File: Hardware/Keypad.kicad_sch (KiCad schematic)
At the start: 35 parts, among them SW1 MX1A-E1NW, SW10 MX1A-E1NW, SW11 MX1A-E1NW, SW12 MX1A-E1NW, SW13 RESET, SW2 MX1A-E1NW, SW3 MX1A-E1NW, SW4 MX1A-E1NW, SW5 MX1A-E1NW, SW6 MX1A-E1NW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

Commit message: minor improvements to PCB design
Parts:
- D13, D14: footprint LED_SMD:LED_0603_1608Metric_Pad1.05x0.95mm_HandSolder -> LED_SMD:LED_0603_1608Metric
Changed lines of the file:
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@@
     (property "Reference" "D14" (id 0) (at 64.77 142.24 0))
     (property "Value" "LED" (id 1) (at 64.77 147.32 0))
-    (property "Footprint" "LED_SMD:LED_0603_1608Metric_Pad1.05x0.95mm_HandSolder" (id 2) (at 64.77 144.78 0)
+    (property "Footprint" "LED_SMD:LED_0603_1608Metric" (id 2) (at 64.77 144.78 0)
       (effects (font (size 1.27 1.27)) hide)
     )
@@
     (property "Reference" "D13" (id 0) (at 64.77 132.08 0))
     (property "Value" "LED" (id 1) (at 64.77 137.16 0))
-    (property "Footprint" "LED_SMD:LED_0603_1608Metric_Pad1.05x0.95mm_HandSolder" (id 2) (at 64.77 134.62 0)
+    (property "Footprint" "LED_SMD:LED_0603_1608Metric" (id 2) (at 64.77 134.62 0)
       (effects (font (size 1.27 1.27)) hide)
     )
@@
     )
     (path "/f4e1b81e-f02a-451a-905f-f000b6b75e92"
-      (reference "D13") (unit 1) (value "LED") (footprint "LED_SMD:LED_0603_1608Metric_Pad1.05x0.95mm_HandSolder")
+      (reference "D13") (unit 1) (value "LED") (footprint "LED_SMD:LED_0603_1608Metric")
     )
     (path "/e7f7fe4f-ebfb-471a-976d-2ea6e6769e03"
-      (reference "D14") (unit 1) (value "LED") (footprint "LED_SMD:LED_0603_1608Metric_Pad1.05x0.95mm_HandSolder")
+      (reference "D14") (unit 1) (value "LED") (footprint "LED_SMD:LED_0603_1608Metric")
     )
     (path "/dc9e1614-34a9-4e22-a9cf-c8e55ec48f0f"

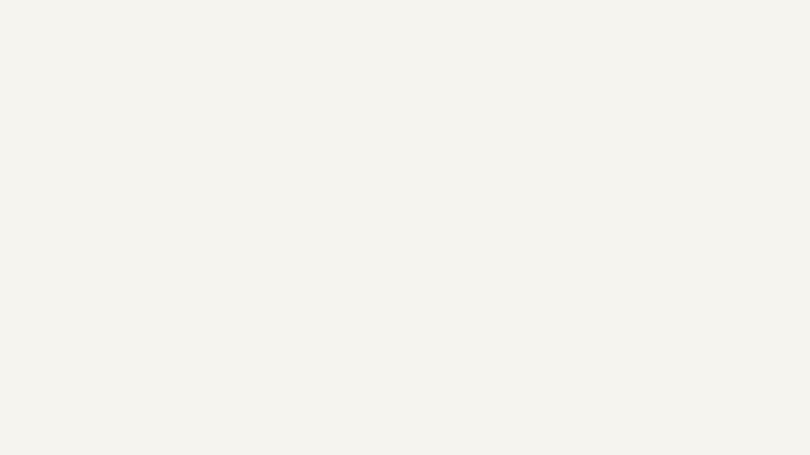
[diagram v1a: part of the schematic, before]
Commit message: replaced mounting holes with grounded pads
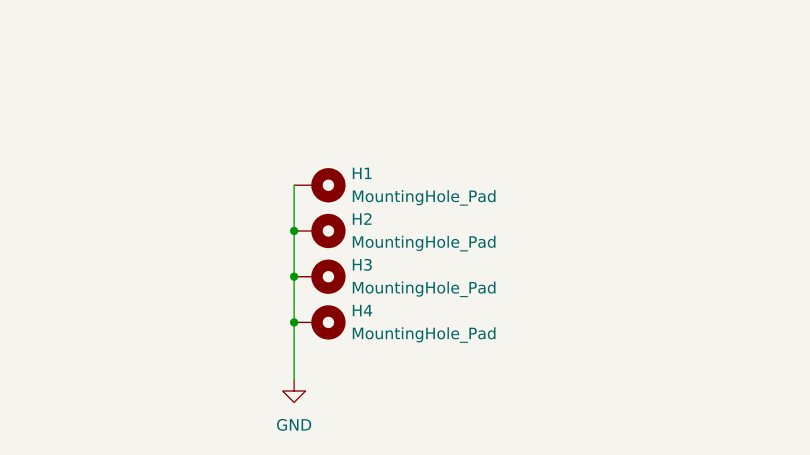
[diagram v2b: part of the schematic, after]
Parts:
- added H1, H2, H3, H4: MountingHole_Pad, MountingHole:MountingHole_2.7mm_M2.5_Pad, symbol Mechanical:MountingHole_Pad
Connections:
- net GND: now also H1.1, H2.1, H3.1, H4.1
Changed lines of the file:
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@@
   (junction (at 198.12 114.3) (diameter 0) (color 0 0 0 0)
   )
+  (junction (at 110.49 175.26) (diameter 0) (color 0 0 0 0)
+  )
   (junction (at 67.31 92.71) (diameter 0) (color 0 0 0 0)
   )
@@
   (junction (at 250.19 87.63) (diameter 0) (color 0 0 0 0)
   )
+  (junction (at 110.49 170.18) (diameter 0) (color 0 0 0 0)
+  )
   (junction (at 85.09 96.52) (diameter 0) (color 0 0 0 0)
   )
@@
   (junction (at 236.22 114.3) (diameter 0) (color 0 0 0 0)
   )
+  (junction (at 110.49 165.1) (diameter 0) (color 0 0 0 0)
+  )
   (junction (at 218.44 106.68) (diameter 0) (color 0 0 0 0)
   )
@@
     (stroke (width 0) (type default) (color 0 0 0 0))
   )
+  (wire (pts (xy 110.49 160.02) (xy 110.49 165.1))
+    (stroke (width 0) (type default) (color 0 0 0 0))
+  )
   (wire (pts (xy 66.04 66.04) (xy 67.31 66.04))
     (stroke (width 0) (type default) (color 0 0 0 0))
@@
     (stroke (width 0) (type default) (color 0 0 0 0))
   )
+  (wire (pts (xy 110.49 175.26) (xy 110.49 181.61))
+    (stroke (width 0) (type default) (color 0 0 0 0))
+  )
   (wire (pts (xy 250.19 72.39) (xy 250.19 87.63))
     (stroke (width 0) (type default) (color 0 0 0 0))
@@
     (stroke (width 0) (type default) (color 0 0 0 0))
   )
+  (wire (pts (xy 110.49 170.18) (xy 110.49 175.26))
+    (stroke (width 0) (type default) (color 0 0 0 0))
+  )
   (wire (pts (xy 198.12 125.73) (xy 195.58 125.73))
     (stroke (width 0) (type default) (color 0 0 0 0))
@@
   )
   (wire (pts (xy 198.12 95.25) (xy 236.22 95.25))
+    (stroke (width 0) (type default) (color 0 0 0 0))
+  )
+  (wire (pts (xy 110.49 165.1) (xy 110.49 170.18))
     (stroke (width 0) (type default) (color 0 0 0 0))
   )
@@
     (pin "2")
   )
+  (symbol (lib_id "Mechanical:MountingHole_Pad") (at 113.03 160.02 270) (unit 1)
+    (in_bom yes) (on_board yes) (fields_autoplaced)
+    (property "Reference" "H1" (id 0) (at 116.84 158.7499 90)
+      (effects (font (size 1.27 1.27)) (justify left))
+    )
+    (property "Value" "MountingHole_Pad" (id 1) (at 116.84 161.2899 90)
+      (effects (font (size 1.27 1.27)) (justify left))
+    )
+    (property "Footprint" "MountingHole:MountingHole_2.7mm_M2.5_Pad" (id 2) (at 113.03 160.02 0)
+      (effects (font (size 1.27 1.27)) hide)
+    )
+    (property "Datasheet" "~" (id 3) (at 113.03 160.02 0)
+      (effects (font (size 1.27 1.27)) hide)
+    )
+    (pin "1")
+  )
   (symbol (lib_id "Diode:1N4148") (at 267.97 110.49 90) (unit 1)
     (in_bom yes) (on_board yes) (fields_autoplaced)
@@
     (pin "2")
   )
+  (symbol (lib_id "power:GND") (at 110.49 181.61 0) (unit 1)
+    (in_bom yes) (on_board yes) (fields_autoplaced)
+    (property "Reference" "#PWR0105" (id 0) (at 110.49 187.96 0)
+      (effects (font (size 1.27 1.27)) hide)
+    )
+    (property "Value" "GND" (id 1) (at 110.49 186.69 0))
+    (property "Footprint" "" (id 2) (at 110.49 181.61 0)
+      (effects (font (size 1.27 1.27)) hide)
+    )
+    (property "Datasheet" "" (id 3) (at 110.49 181.61 0)
+      (effects (font (size 1.27 1.27)) hide)
+    )
+    (pin "1")
+  )
   (symbol (lib_id "Diode:1N4148") (at 236.22 129.54 90) (unit 1)
     (in_bom yes) (on_board yes) (fields_autoplaced)
@@
     (pin "1")
     (pin "2")
+  )
+  (symbol (lib_id "Mechanical:MountingHole_Pad") (at 113.03 170.18 270) (unit 1)
+    (in_bom yes) (on_board yes) (fields_autoplaced)
+    (property "Reference" "H3" (id 0) (at 116.84 168.9099 90)
+      (effects (font (size 1.27 1.27)) (justify left))
+    )
+    (property "Value" "MountingHole_Pad" (id 1) (at 116.84 171.4499 90)
+      (effects (font (size 1.27 1.27)) (justify left))
+    )
+    (property "Footprint" "MountingHole:MountingHole_2.7mm_M2.5_Pad" (id 2) (at 113.03 170.18 0)
+      (effects (font (size 1.27 1.27)) hide)
+    )
+    (property "Datasheet" "~" (id 3) (at 113.03 170.18 0)
+      (effects (font (size 1.27 1.27)) hide)
+    )
+    (pin "1")
   )
   (symbol (lib_id "Switch:SW_Push") (at 60.96 66.04 0) (unit 1)
@@
     (pin "2")
   )
+  (symbol (lib_id "Mechanical:MountingHole_Pad") (at 113.03 175.26 270) (unit 1)
+    (in_bom yes) (on_board yes) (fields_autoplaced)
+    (property "Reference" "H4" (id 0) (at 116.84 173.9899 90)
+      (effects (font (size 1.27 1.27)) (justify left))
+    )
+    (property "Value" "MountingHole_Pad" (id 1) (at 116.84 176.5299 90)
+      (effects (font (size 1.27 1.27)) (justify left))
+    )
+    (property "Footprint" "MountingHole:MountingHole_2.7mm_M2.5_Pad" (id 2) (at 113.03 175.26 0)
+      (effects (font (size 1.27 1.27)) hide)
+    )
+    (property "Datasheet" "~" (id 3) (at 113.03 175.26 0)
+      (effects (font (size 1.27 1.27)) hide)
+    )
+    (pin "1")
+  )
   (symbol (lib_id "power:+3V3") (at 85.09 96.52 0) (unit 1)
     (in_bom yes) (on_board yes) (fields_autoplaced)
@@
     )
     (property "Datasheet" "" (id 3) (at 85.09 96.52 0)
+      (effects (font (size 1.27 1.27)) hide)
+    )
+    (pin "1")
+  )
+  (symbol (lib_id "Mechanical:MountingHole_Pad") (at 113.03 165.1 270) (unit 1)
+    (in_bom yes) (on_board yes) (fields_autoplaced)
+    (property "Reference" "H2" (id 0) (at 116.84 163.8299 90)
+      (effects (font (size 1.27 1.27)) (justify left))
+    )
+    (property "Value" "MountingHole_Pad" (id 1) (at 116.84 166.3699 90)
+      (effects (font (size 1.27 1.27)) (justify left))
+    )
+    (property "Footprint" "MountingHole:MountingHole_2.7mm_M2.5_Pad" (id 2) (at 113.03 165.1 0)
+      (effects (font (size 1.27 1.27)) hide)
+    )
+    (property "Datasheet" "~" (id 3) (at 113.03 165.1 0)
       (effects (font (size 1.27 1.27)) hide)
     )
@@
       (reference "#PWR0104") (unit 1) (value "GND") (footprint "")
     )
+    (path "/4c41d73b-9629-4891-9f71-d307bc169690"
+      (reference "#PWR0105") (unit 1) (value "GND") (footprint "")
+    )
     (path "/9b5a0617-70c8-4bdd-b9f5-190c8f0a9438"
       (reference "D1") (unit 1) (value "1N4148") (footprint "Diode_SMD:D_MELF")
@@
       (reference "D14") (unit 1) (value "LED") (footprint "LED_SMD:LED_0603_1608Metric")
     )
+    (path "/2abf9bd9-2e75-4bc7-9218-8b355c67c085"
+      (reference "H1") (unit 1) (value "MountingHole_Pad") (footprint "MountingHole:MountingHole_2.7mm_M2.5_Pad")
+    )
+    (path "/abba4978-3a4b-4852-b54b-6b91e24103c3"
+      (reference "H2") (unit 1) (value "MountingHole_Pad") (footprint "MountingHole:MountingHole_2.7mm_M2.5_Pad")
+    )
+    (path "/75202622-1795-44f1-83e8-a3062aaae217"
+      (reference "H3") (unit 1) (value "MountingHole_Pad") (footprint "MountingHole:MountingHole_2.7mm_M2.5_Pad")
+    )
+    (path "/9f0df0db-34ed-4aca-8400-a4bc646665f9"
+      (reference "H4") (unit 1) (value "MountingHole_Pad") (footprint "MountingHole:MountingHole_2.7mm_M2.5_Pad")
+    )
     (path "/dc9e1614-34a9-4e22-a9cf-c8e55ec48f0f"

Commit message: updated diode footprints to MiniMELF
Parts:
- D1, D10, D11, D12, D2, D3, D4, D5, D6, D7, D8, D9: footprint Diode_SMD:D_MELF -> Diode_SMD:D_MiniMELF
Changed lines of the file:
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@@
       (effects (font (size 1.27 1.27)) (justify right))
     )
-    (property "Footprint" "Diode_SMD:D_MELF" (id 2) (at 272.415 129.54 0)
+    (property "Footprint" "Diode_SMD:D_MiniMELF" (id 2) (at 272.415 129.54 0)
       (effects (font (size 1.27 1.27)) hide)
     )
@@
       (effects (font (size 1.27 1.27)) (justify right))
     )
-    (property "Footprint" "Diode_SMD:D_MELF" (id 2) (at 272.415 110.49 0)
+    (property "Footprint" "Diode_SMD:D_MiniMELF" (id 2) (at 272.415 110.49 0)
       (effects (font (size 1.27 1.27)) hide)
     )
@@
       (effects (font (size 1.27 1.27)) (justify right))
     )
-    (property "Footprint" "Diode_SMD:D_MELF" (id 2) (at 240.665 129.54 0)
+    (property "Footprint" "Diode_SMD:D_MiniMELF" (id 2) (at 240.665 129.54 0)
       (effects (font (size 1.27 1.27)) hide)
     )
@@
       (effects (font (size 1.27 1.27)) (justify right))
     )
-    (property "Footprint" "Diode_SMD:D_MELF" (id 2) (at 202.565 91.44 0)
+    (property "Footprint" "Diode_SMD:D_MiniMELF" (id 2) (at 202.565 91.44 0)
       (effects (font (size 1.27 1.27)) hide)
     )
@@
       (effects (font (size 1.27 1.27)) (justify right))
     )
-    (property "Footprint" "Diode_SMD:D_MELF" (id 2) (at 164.465 91.44 0)
+    (property "Footprint" "Diode_SMD:D_MiniMELF" (id 2) (at 164.465 91.44 0)
       (effects (font (size 1.27 1.27)) hide)
     )
@@
       (effects (font (size 1.27 1.27)) (justify right))
     )
-    (property "Footprint" "Diode_SMD:D_MELF" (id 2) (at 164.465 110.49 0)
+    (property "Footprint" "Diode_SMD:D_MiniMELF" (id 2) (at 164.465 110.49 0)
       (effects (font (size 1.27 1.27)) hide)
     )
@@
       (effects (font (size 1.27 1.27)) (justify right))
     )
-    (property "Footprint" "Diode_SMD:D_MELF" (id 2) (at 202.565 110.49 0)
+    (property "Footprint" "Diode_SMD:D_MiniMELF" (id 2) (at 202.565 110.49 0)
       (effects (font (size 1.27 1.27)) hide)
     )
@@
       (effects (font (size 1.27 1.27)) (justify right))
     )
-    (property "Footprint" "Diode_SMD:D_MELF" (id 2) (at 272.415 91.44 0)
+    (property "Footprint" "Diode_SMD:D_MiniMELF" (id 2) (at 272.415 91.44 0)
       (effects (font (size 1.27 1.27)) hide)
     )
@@
       (effects (font (size 1.27 1.27)) (justify right))
     )
-    (property "Footprint" "Diode_SMD:D_MELF" (id 2) (at 240.665 110.49 0)
+    (property "Footprint" "Diode_SMD:D_MiniMELF" (id 2) (at 240.665 110.49 0)
       (effects (font (size 1.27 1.27)) hide)
     )
@@
       (effects (font (size 1.27 1.27)) (justify right))
     )
-    (property "Footprint" "Diode_SMD:D_MELF" (id 2) (at 240.665 91.44 0)
+    (property "Footprint" "Diode_SMD:D_MiniMELF" (id 2) (at 240.665 91.44 0)
       (effects (font (size 1.27 1.27)) hide)
     )
@@
       (effects (font (size 1.27 1.27)) (justify right))
     )
-    (property "Footprint" "Diode_SMD:D_MELF" (id 2) (at 202.565 129.54 0)
+    (property "Footprint" "Diode_SMD:D_MiniMELF" (id 2) (at 202.565 129.54 0)
       (effects (font (size 1.27 1.27)) hide)
     )
@@
       (effects (font (size 1.27 1.27)) (justify right))
     )
-    (property "Footprint" "Diode_SMD:D_MELF" (id 2) (at 164.465 129.54 0)
+    (property "Footprint" "Diode_SMD:D_MiniMELF" (id 2) (at 164.465 129.54 0)
       (effects (font (size 1.27 1.27)) hide)
     )
@@
     )
     (path "/9b5a0617-70c8-4bdd-b9f5-190c8f0a9438"
-      (reference "D1") (unit 1) (value "1N4148") (footprint "Diode_SMD:D_MELF")
+      (reference "D1") (unit 1) (value "1N4148") (footprint "Diode_SMD:D_MiniMELF")
     )
     (path "/b248ebf8-e66a-48dd-9ffc-1b48dd041fa4"
-      (reference "D2") (unit 1) (value "1N4148") (footprint "Diode_SMD:D_MELF")
+      (reference "D2") (unit 1) (value "1N4148") (footprint "Diode_SMD:D_MiniMELF")
     )
     (path "/f5a280e2-fe94-447b-91da-9bdd2415b650"
-      (reference "D3") (unit 1) (value "1N4148") (footprint "Diode_SMD:D_MELF")
+      (reference "D3") (unit 1) (value "1N4148") (footprint "Diode_SMD:D_MiniMELF")
     )
     (path "/4e9bd388-6e4e-40b6-94bc-0efcfe1e5f39"
-      (reference "D4") (unit 1) (value "1N4148") (footprint "Diode_SMD:D_MELF")
+      (reference "D4") (unit 1) (value "1N4148") (footprint "Diode_SMD:D_MiniMELF")
     )
     (path "/ba29d218-4597-4401-b91a-b89c5c4a70fe"
-      (reference "D5") (unit 1) (value "1N4148") (footprint "Diode_SMD:D_MELF")
+      (reference "D5") (unit 1) (value "1N4148") (footprint "Diode_SMD:D_MiniMELF")
     )
     (path "/d3c483b2-b4e3-402a-b140-8d1dba00b8ff"
-      (reference "D6") (unit 1) (value "1N4148") (footprint "Diode_SMD:D_MELF")
+      (reference "D6") (unit 1) (value "1N4148") (footprint "Diode_SMD:D_MiniMELF")
     )
     (path "/d34dadda-af54-47cc-afb5-65c048f49f68"
-      (reference "D7") (unit 1) (value "1N4148") (footprint "Diode_SMD:D_MELF")
+      (reference "D7") (unit 1) (value "1N4148") (footprint "Diode_SMD:D_MiniMELF")
     )
     (path "/d346cbd1-3b78-439b-a8ce-39f202c00287"
-      (reference "D8") (unit 1) (value "1N4148") (footprint "Diode_SMD:D_MELF")
+      (reference "D8") (unit 1) (value "1N4148") (footprint "Diode_SMD:D_MiniMELF")
     )
     (path "/4e55e41a-1719-4b14-bd05-18e6fd5307d8"
-      (reference "D9") (unit 1) (value "1N4148") (footprint "Diode_SMD:D_MELF")
+      (reference "D9") (unit 1) (value "1N4148") (footprint "Diode_SMD:D_MiniMELF")
     )
     (path "/c089e6e2-72f2-45a4-b879-d69ea7934dd2"
-      (reference "D10") (unit 1) (value "1N4148") (footprint "Diode_SMD:D_MELF")
+      (reference "D10") (unit 1) (value "1N4148") (footprint "Diode_SMD:D_MiniMELF")
     )
     (path "/2c680e31-1c6e-4bd4-ba74-3216e624040b"
-      (reference "D11") (unit 1) (value "1N4148") (footprint "Diode_SMD:D_MELF")
+      (reference "D11") (unit 1) (value "1N4148") (footprint "Diode_SMD:D_MiniMELF")
     )
     (path "/26b83277-fc6a-46f7-b2ad-7b48397191fb"
-      (reference "D12") (unit 1) (value "1N4148") (footprint "Diode_SMD:D_MELF")
+      (reference "D12") (unit 1) (value "1N4148") (footprint "Diode_SMD:D_MiniMELF")
     )
     (path "/f4e1b81e-f02a-451a-905f-f000b6b75e92"
